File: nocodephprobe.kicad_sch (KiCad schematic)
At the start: 37 parts, among them J1 BNC (pH Probe), J2 10K, Q1 2N7002, SW1 SW_SPST, U1 TLV272, U2 ICL7106CPL, U3 MCP1501T-10E/CHY, U4 VI-302-DP-RC-S

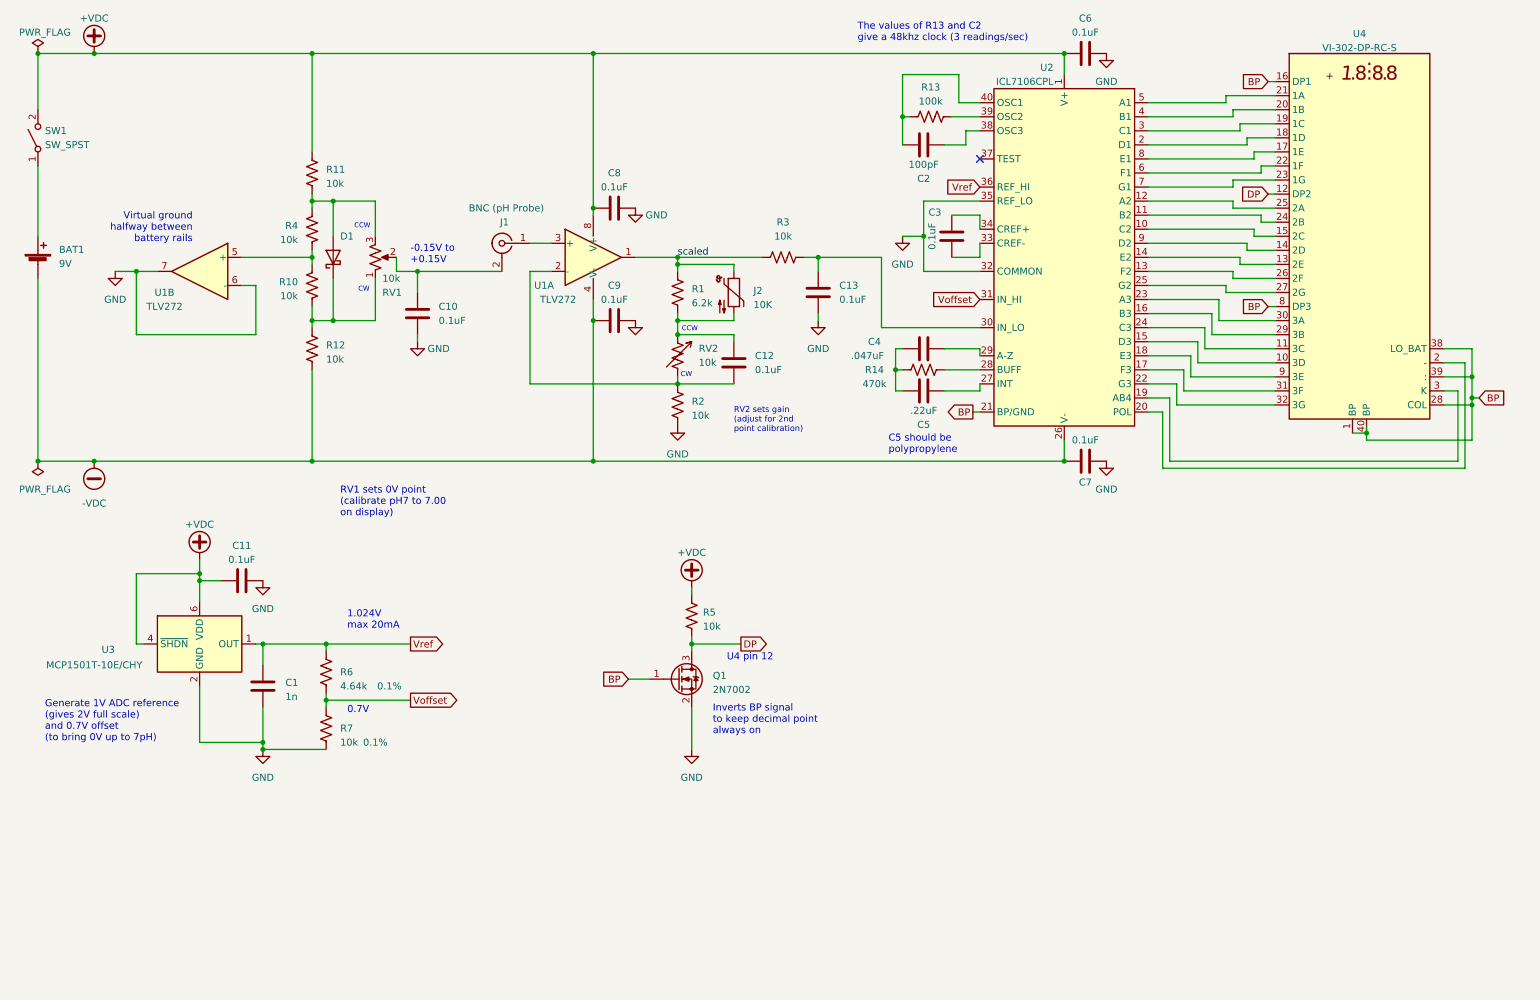
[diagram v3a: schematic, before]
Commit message: Implement [optional] input protection
D2 will clamp the input to 3 diode drops from either rail (~1.8V). This
keeps the input within the safe range for the TLV272. R15 limits the
current in case of overvoltage. The diodes in D3 and D4 set a bias point
two diode drops below the positive rail and above the negative rail to
minimize the reverse voltage (and therefore leakage current) across the
D2 diodes.

Since the D2 diodes are reverse-biased normally, they should not affect
normal input. However, the tricky part is finding diodes with low enough
(preferabley <10pA) reverse leakage current. These BAV199 diodes are by
far the most cost effective solution I found ($0.18 in single quantities
of dual diodes); they have a typical
leakage current of only 3pA @75V (so probably much less at ~2V) -- but
they are only guaranteed to be less than 5nA which is way too high. So
technically they should be characterized before using them in circuit.

Other potential solutions:
- diode-connected JFET like the MMBF4117 with max 10pA Igss
  (https://www.digikey.com/en/products/detail/onsemi/MMBF4117/1049290).
  But these are $1-$5 each.
- diode-connect BJTs like the 2N3904 are supposed to be very low
  leakage. These are cheap, but I'd have to experiment with them.

I think it is generally safe to leave off the protection diodes all
together (but might as well leave R15; it barely contributes to input
impedance). But if you do, I'd recommend connecting the probe to the
meter before powerint it on just to make sure the input of the op-amp
does not float above its rails. The TLV272 and other op-amps with low
current bias seem to have no or minimal static protection.
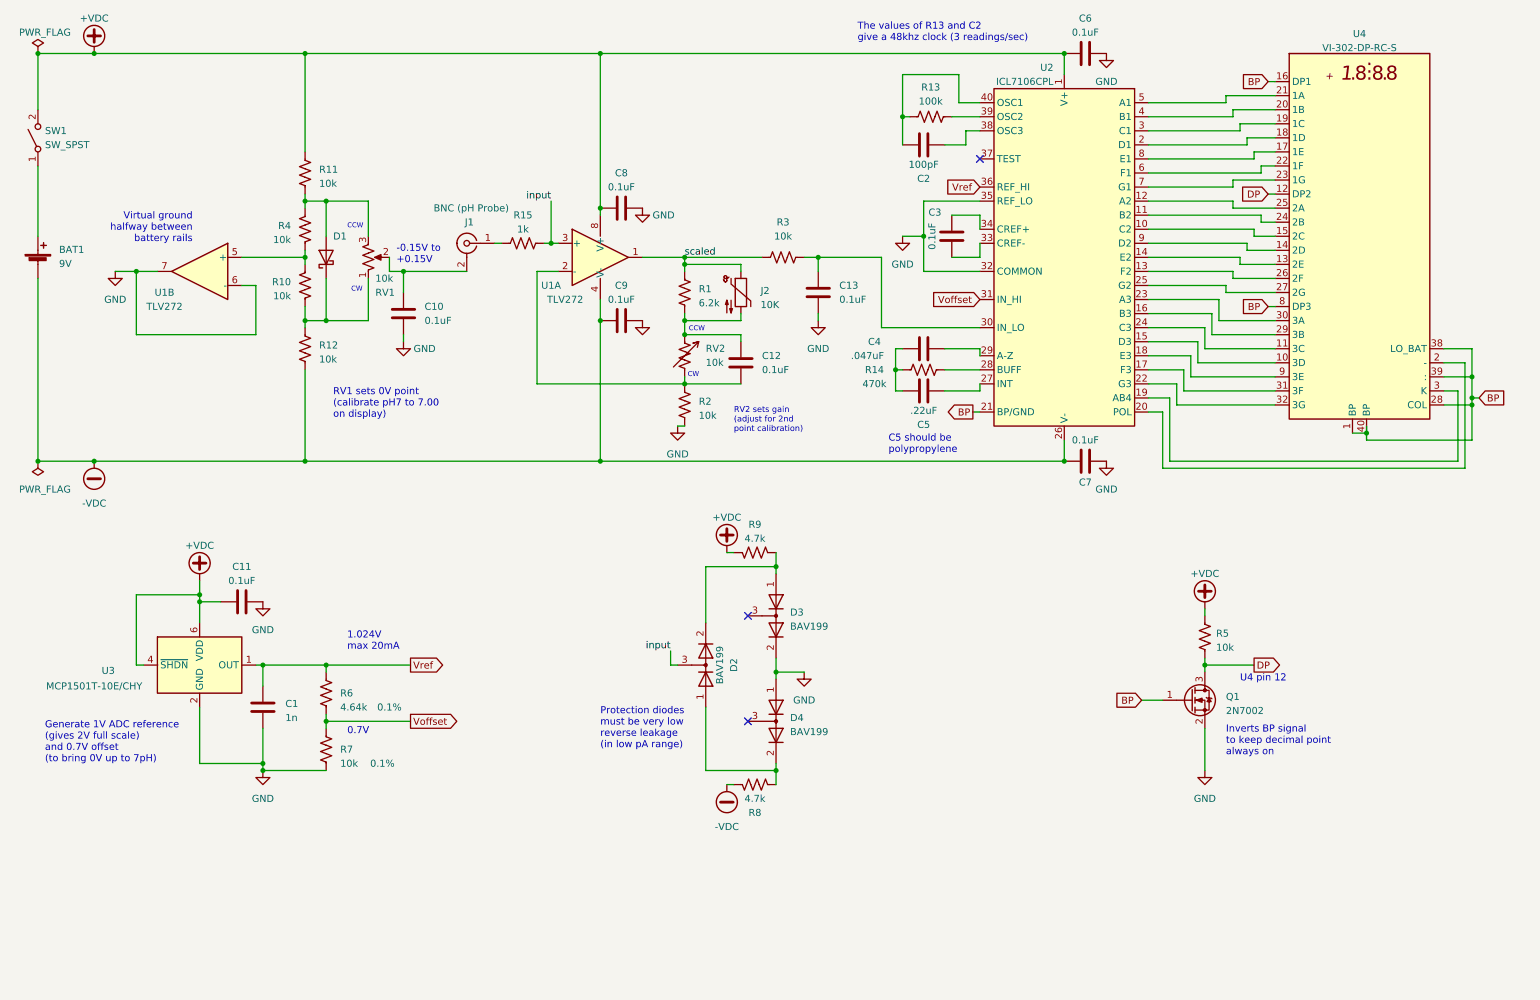
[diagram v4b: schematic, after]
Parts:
- added D2, D3, D4: BAV199, Package_TO_SOT_SMD:SOT-23, symbol Device:D_Dual_Series_CAK
- added R15: 1k, Resistor_SMD:R_0805_2012Metric_Pad1.20x1.40mm_HandSolder, symbol Device:R_US
- added R8, R9: 4.7k, Resistor_SMD:R_0805_2012Metric_Pad1.20x1.40mm_HandSolder, symbol Device:R_US
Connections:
- net +VDC: now also R9.1
- net -VDC: now also R8.2
- net GND: now also D3.2 (K), D4.1 (A)
- net at J1.1 (In): now also R15.2; no longer U1.3 (+)
- new net: D2.1 (A), D4.2 (K), R8.1
- new net: D2.2 (K), D3.1 (A), R9.2
- new net input: D2.3 (common), R15.1, U1.3 (+)
- no-connect marks 1 -> 3
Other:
- note added: "Protection diodes must be very low reverse leakage (in low pA range)"
- moved on the sheet: C1, C10, C11, C12, C8, C9, D1, J1, J2, Q1, R1, R10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

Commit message: Specify cheaper Schottky diodes
Also add one as reverse-voltage protection to protect op-amp input (D5)
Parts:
- added D5: BAT54-Q, Package_TO_SOT_SMD:TSOT-23_HandSoldering, symbol Device:D_Schottky
- D1: value SS14 -> BAT54-Q; footprint Diode_SMD:D_SMA -> Package_TO_SOT_SMD:TSOT-23_HandSoldering
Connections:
- net at SW1.1 (A): now also D5.3 (nc); no longer BAT1.1 (+)
- net at R10.1, R12.2, RV1.1: now also D1.3 (nc); no longer D1.1 (K)
- net at R11.1, R4.2, RV1.3: now also D1.1 (A); no longer D1.2 (A)
- new net: BAT1.1 (+), D5.1 (A)
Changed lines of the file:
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@@
+    (stroke (width 0) (type default))
+  )
+  (wire (pts (xy 16.51 55.88) (xy 16.51 59.69))
     (stroke (width 0) (type default))
   )
@@
     (stroke (width 0) (type default))
   )
-  (wire (pts (xy 16.51 46.99) (xy 16.51 59.69))
+  (wire (pts (xy 16.51 46.99) (xy 16.51 48.26))
     (stroke (width 0) (type default))
   )
@@
     )
   )
+  (symbol (lib_id "Device:D_Schottky") (at 16.51 52.07 270) (unit 1)
+    (in_bom yes) (on_board yes) (dnp no)
+    (property "Reference" "D5" (at 21.59 52.07 90)
+      (effects (font (size 1.27 1.27)) (justify right))
+    )
+    (property "Value" "BAT54-Q" (at 13.97 53.34 0)
+      (effects (font (size 1.27 1.27)) (justify right) hide)
+    )
+    (property "Footprint" "Package_TO_SOT_SMD:TSOT-23_HandSoldering" (at 11.43 53.34 0)
+      (effects (font (size 1.27 1.27)) hide)
+    )
+    (property "Datasheet" "~" (at 16.51 52.07 0)
+      (effects (font (size 1.27 1.27)) hide)
+    )
+    (property "Sim.Device" "D" (at 16.51 52.07 0)
+      (effects (font (size 1.27 1.27)) hide)
+    )
+    (property "Sim.Pins" "1=A 3=K" (at 19.05 52.07 0)
+      (effects (font (size 1.27 1.27)) hide)
+    )
+    (pin "1")
+    (pin "3")
+    (pin "3")
+    (instances
+      (project "nocodephprobe"
+        (path "/2036f74b-8ede-4e4d-84df-8cc119de9ab1"
+          (reference "D5") (unit 1)
+        )
+      )
+    )
+  )
   (symbol (lib_id "Device:Thermistor_NTC") (at 143.51 69.85 0) (unit 1)
     (in_bom yes) (on_board yes) (dnp no) (fields_autoplaced)
@@
       (effects (font (size 1.27 1.27)) (justify right))
     )
-    (property "Value" "SS14" (at 71.12 62.23 0)
+    (property "Value" "BAT54-Q" (at 71.12 62.23 0)
       (effects (font (size 1.27 1.27)) (justify right) hide)
     )
-    (property "Footprint" "Diode_SMD:D_SMA" (at 68.58 63.5 0)
+    (property "Footprint" "Package_TO_SOT_SMD:TSOT-23_HandSoldering" (at 73.66 62.23 0)
       (effects (font (size 1.27 1.27)) hide)
     )
@@
       (effects (font (size 1.27 1.27)) hide)
     )
-    (property "Sim.Pins" "1=K 2=A" (at 68.58 63.5 0)
-      (effects (font (size 1.27 1.27)) hide)
-    )
-    (pin "1")
-    (pin "2")
-    (instances
-      (project "nocodephprobe"
+    (property "Sim.Pins" "1=A 3=K" (at 66.04 63.5 0)
+      (effects (font (size 1.27 1.27)) hide)
+    )
+    (pin "1")
+    (pin "3")
+    (pin "3")
+    (instances
+      (project "nocodephprobe"

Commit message: Use SPDT for power switch
I decided on these MTS-103 mini toggle switches, to be mounted next to BNC
(and connected with wires to JST XH connector):

https://www.amazon.com/dp/B07CJFVZ7M
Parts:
- SW1: symbol Switch:SW_SPST -> Switch:SW_SPDT
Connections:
- no-connect marks 3 -> 4
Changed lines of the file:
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@@
   (no_connect (at 144.78 128.27))
   (no_connect (at 186.69 45.72))
+  (no_connect (at 13.97 36.83))
   (wire (pts (xy 176.53 66.04) (xy 186.69 66.04))
     (stroke (width 0) (type default))
@@
   )
   (wire (pts (xy 270.51 80.01) (xy 275.59 80.01))
+    (stroke (width 0) (type default))
+  )
+  (wire (pts (xy 16.51 36.83) (xy 19.05 36.83))
     (stroke (width 0) (type default))
   )
@@
     )
   )
-  (symbol (lib_id "Switch:SW_SPST") (at 16.51 41.91 90) (unit 1)
+  (symbol (lib_id "Switch:SW_SPDT") (at 16.51 41.91 90) (unit 1)
     (in_bom yes) (on_board yes) (dnp no)
-    (property "Reference" "SW1" (at 17.78 40.64 90)
+    (property "Reference" "SW1" (at 21.59 41.91 90)
       (effects (font (size 1.27 1.27)) (justify right))
     )
-    (property "Value" "SW_SPST" (at 17.78 43.18 90)
+    (property "Value" "SW_SPST" (at 21.59 44.45 90)
       (effects (font (size 1.27 1.27)) (justify right))
     )
@@
       (effects (font (size 1.27 1.27)) hide)
     )
+    (pin "3")
     (pin "1")
     (pin "2")

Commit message: Revert to using 3-pin connector for RV2
I think it is more flexible. Can always use a 3-pin plug with only 2
wires populated.
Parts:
- RV2: footprint Connector_JST:JST_XH_B2B-XH-A_1x02_P2.50mm_Vertical -> Connector_JST:JST_XH_B3B-XH-A_1x03_P2.50mm_Vertical; symbol Device:R_Variable_US -> Device:R_Potentiometer_US
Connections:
- net at C12.1, R2.2, U1.2 (-): now also RV2.1; no longer RV2.2
- net at C12.2, J2.5, R1.1: now also RV2.2, RV2.3; no longer RV2.1
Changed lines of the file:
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@@
+    (stroke (width 0) (type default))
+  )
+  (wire (pts (xy 129.54 77.47) (xy 133.35 77.47))
     (stroke (width 0) (type default))
   )
@@
   )
   (wire (pts (xy 168.91 63.5) (xy 168.91 76.2))
+    (stroke (width 0) (type default))
+  )
+  (wire (pts (xy 129.54 81.28) (xy 129.54 77.47))
     (stroke (width 0) (type default))
   )
@@
       (effects (font (size 1.27 1.27)) hide)
     )
+    (pin "1")
+    (pin "2")
     (pin "3")
-    (pin "1")
-    (pin "2")
     (instances
       (project "nocodephprobe"
@@
     )
   )
-  (symbol (lib_id "Device:R_Variable_US") (at 133.35 81.28 0) (unit 1)
+  (symbol (lib_id "Device:R_Potentiometer_US") (at 133.35 81.28 180) (unit 1)
     (in_bom yes) (on_board yes) (dnp no)
-    (property "Reference" "RV2" (at 137.16 79.9719 0)
+    (property "Reference" "RV2" (at 129.54 82.5881 0)
       (effects (font (size 1.27 1.27)) (justify left))
     )
-    (property "Value" "10k" (at 137.16 82.5119 0)
+    (property "Value" "10k" (at 129.54 80.0481 0)
       (effects (font (size 1.27 1.27)) (justify left))
     )
-    (property "Footprint" "Connector_JST:JST_XH_B2B-XH-A_1x02_P2.50mm_Vertical" (at 131.572 81.28 90)
+    (property "Footprint" "Connector_JST:JST_XH_B3B-XH-A_1x03_P2.50mm_Vertical" (at 133.35 81.28 0)
       (effects (font (size 1.27 1.27)) hide)
     )
@@
     (pin "1")
     (pin "2")
-    (instances
-      (project "nocodephprobe"
+    (pin "3")
+    (instances
+      (project "nocodephprobe"
